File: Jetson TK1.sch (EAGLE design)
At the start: 2 parts, among them J3A1 TK1_GPIO_2X25, J3A2 TK1_GPIO_3X25

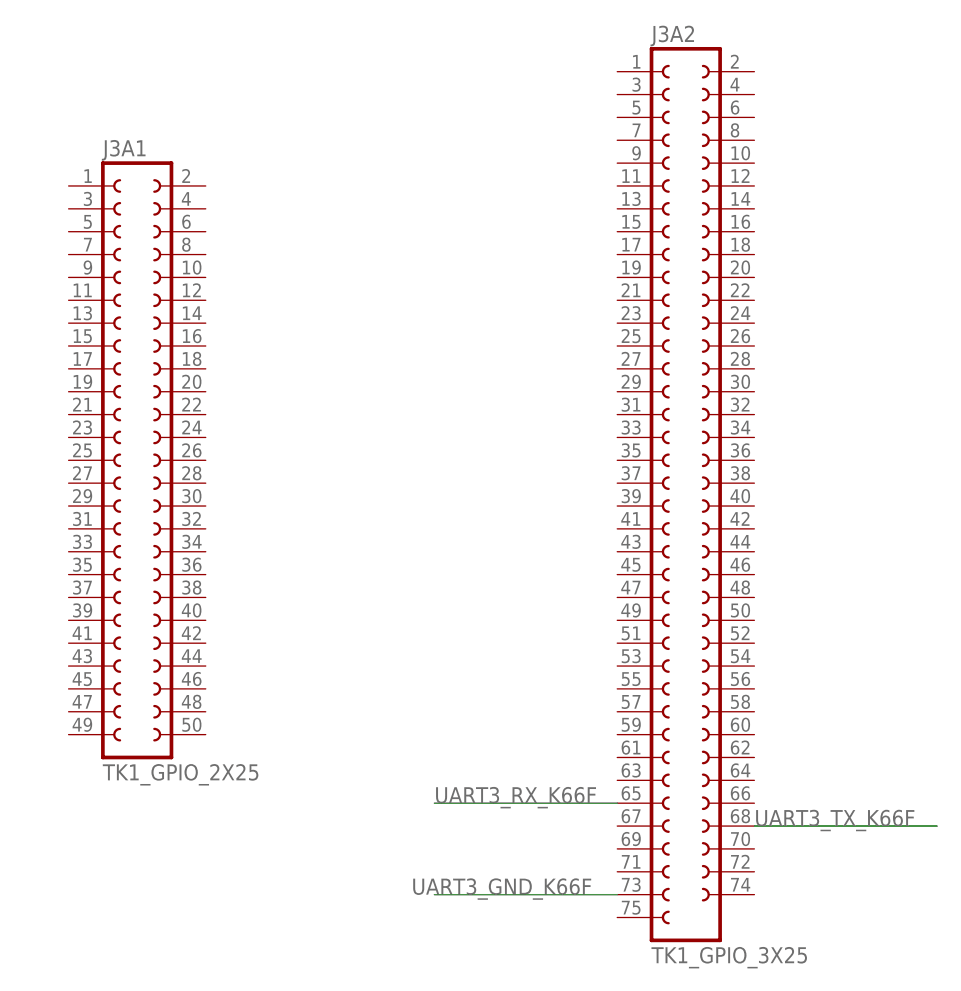
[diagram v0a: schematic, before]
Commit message: Improving part naming convention / Add Proto Schematic
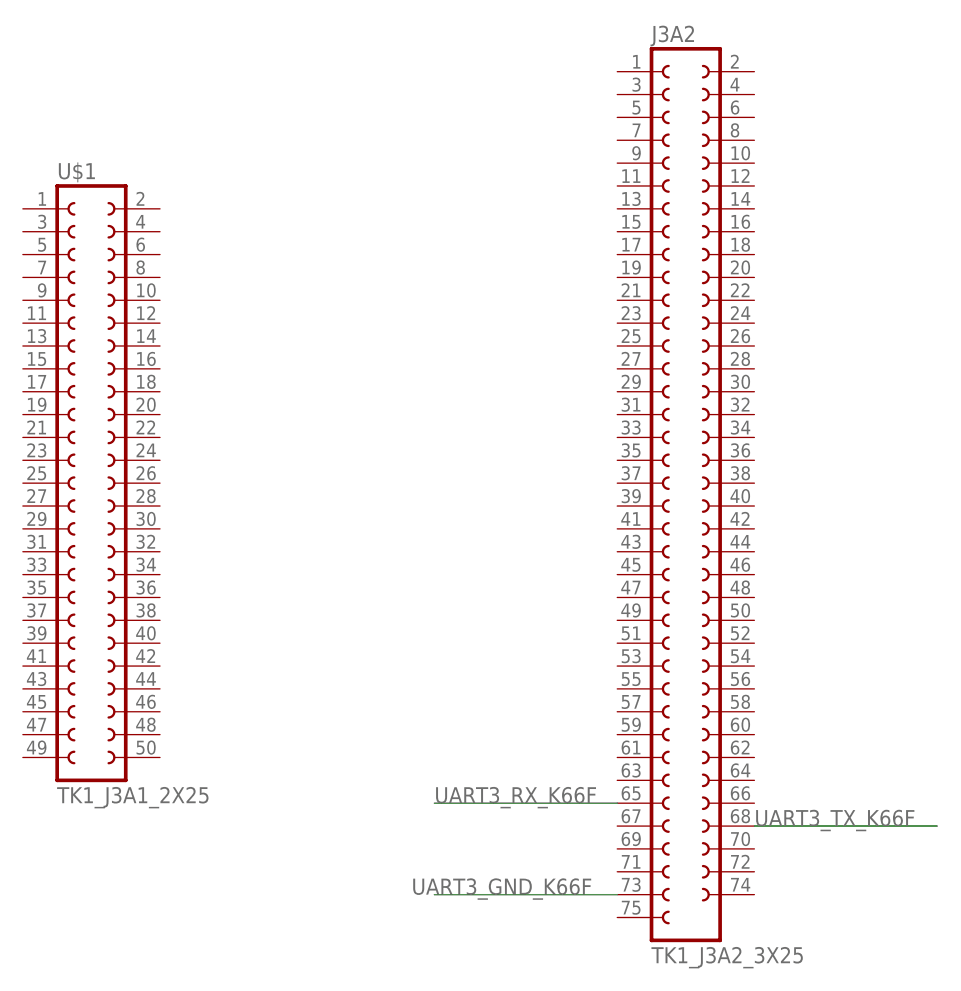
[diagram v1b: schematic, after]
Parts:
- removed J3A1: TK1_GPIO_2X25, Parts:TK1_GPIO_2X25
- added U$1: TK1_J3A1_2X25, Parts:TK1_J3A1_2X25
- J3A2: value TK1_GPIO_3X25 -> TK1_J3A2_3X25; device Parts:TK1_GPIO_3X25 -> Parts:TK1_J3A2_3X25
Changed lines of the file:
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@@
 </classes>
 <parts>
-<part name="J3A1" library="Parts" deviceset="TK1_GPIO_2X25" device=""/>
-<part name="J3A2" library="Parts" deviceset="TK1_GPIO_3X25" device=""/>
+<part name="J3A2" library="Parts" deviceset="TK1_J3A2_3X25" device=""/>
+<part name="U$1" library="Parts" deviceset="TK1_J3A1_2X25" device=""/>
 </parts>
 <sheets>
@@
 </plain>
 <instances>
-<instance part="J3A1" gate="G$1" x="20.32" y="50.8"/>
 <instance part="J3A2" gate="G$1" x="81.28" y="45.72"/>
+<instance part="U$1" gate="G$1" x="15.24" y="48.26"/>
 </instances>
 <busses>
@@
 <net name="UART3_GND_K66F" class="0">
 <segment>
-<pinref part="J3A2" gate="G$1" pin="73"/>
 <wire x1="73.66" y1="0" x2="53.34" y2="0" width="0.1524" layer="91"/>
 <label x="50.8" y="0" size="1.778" layer="95"/>
+<pinref part="J3A2" gate="G$1" pin="73"/>
 </segment>
 </net>
 <net name="UART3_TX_K66F" class="0">
 <segment>
-<pinref part="J3A2" gate="G$1" pin="68"/>
 <wire x1="88.9" y1="7.62" x2="109.22" y2="7.62" width="0.1524" layer="91"/>
 <label x="88.9" y="7.62" size="1.778" layer="95"/>
+<pinref part="J3A2" gate="G$1" pin="68"/>
 </segment>
 </net>
 <net name="UART3_RX_K66F" class="0">
 <segment>
-<pinref part="J3A2" gate="G$1" pin="65"/>
 <wire x1="73.66" y1="10.16" x2="53.34" y2="10.16" width="0.1524" layer="91"/>
 <label x="53.34" y="10.16" size="1.778" layer="95"/>
+<pinref part="J3A2" gate="G$1" pin="65"/>
 </segment>
 </net>
